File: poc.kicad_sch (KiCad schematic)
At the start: 1 part, among them U1 ESP32-S3-WROOM-1

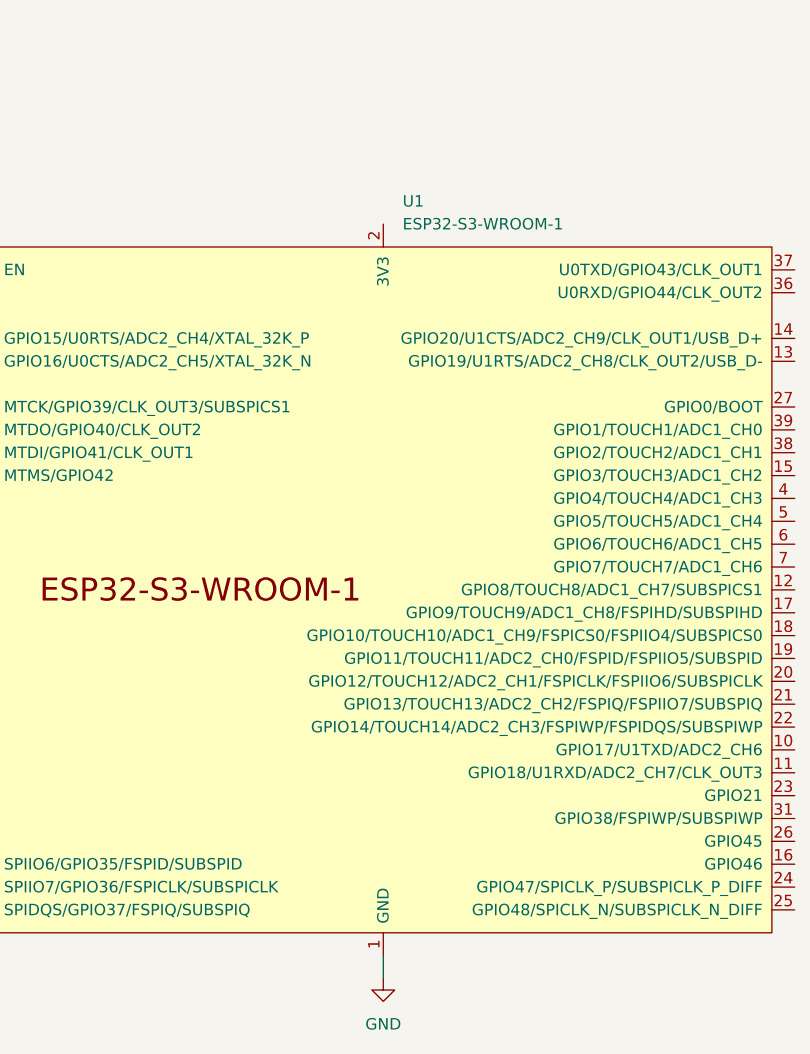
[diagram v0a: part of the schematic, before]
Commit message: POC(schem): add ESP32-S3 power
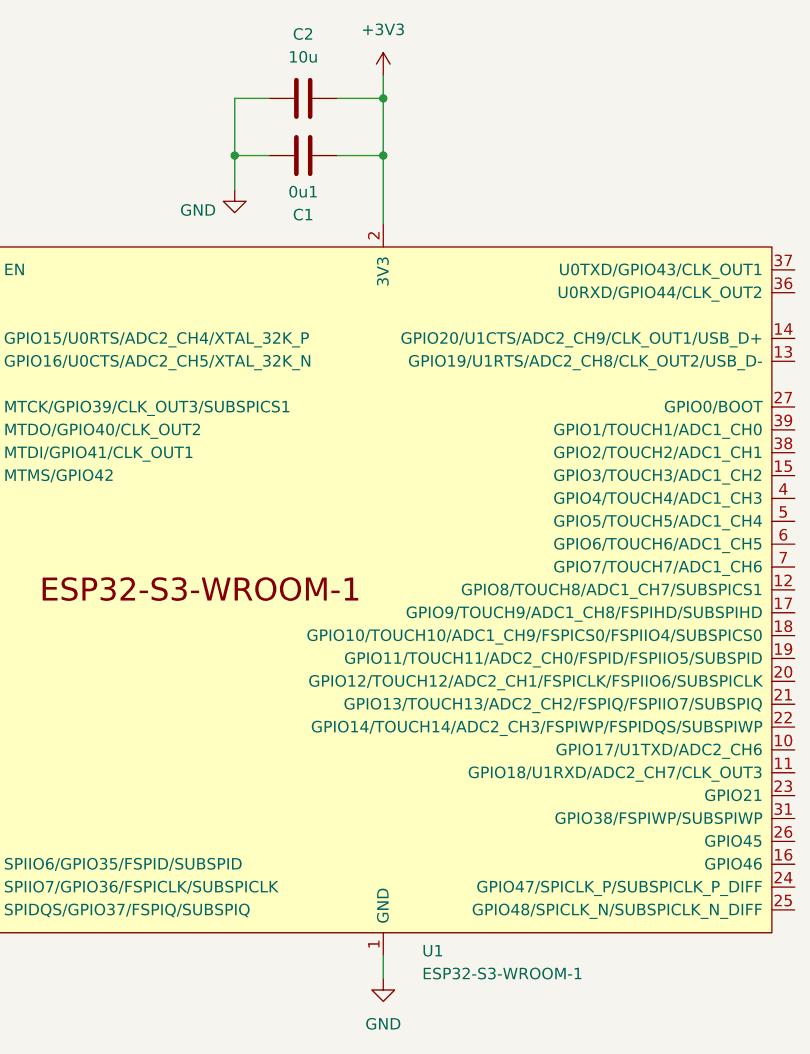
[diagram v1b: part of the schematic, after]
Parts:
- added C1: 0u1, symbol Device:C
- added C2: 10u, symbol Device:C
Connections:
- net GND: now also C1.1, C2.1
- net +3V3: now reaches U1.2 (3V3)
- net +3V3: now also C1.2, C2.2

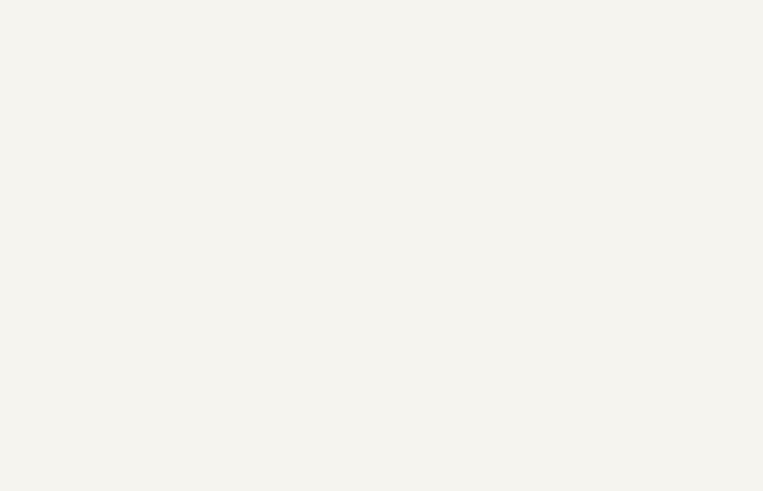
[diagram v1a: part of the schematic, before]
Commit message: POC(schem): add AP7361C 3V3 ldo
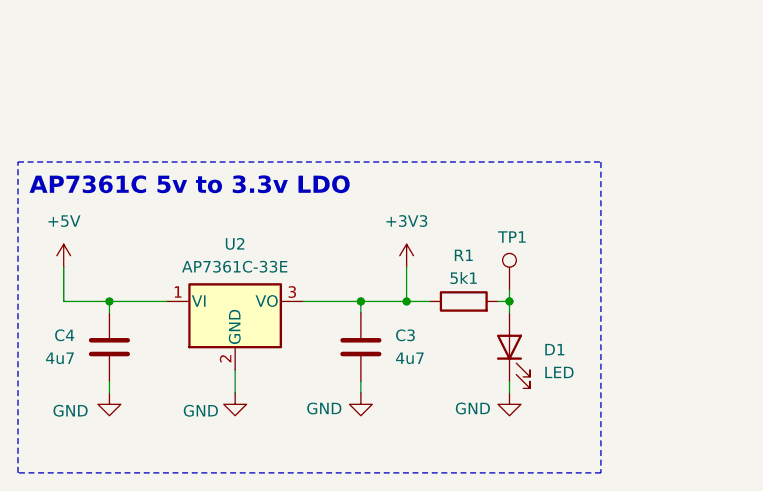
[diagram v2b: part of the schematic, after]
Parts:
- added C3, C4: 4u7, symbol Device:C
- added D1: LED, symbol Device:LED
- added R1: 5k1, symbol Device:R
- added TP1: TestPoint, symbol Connector:TestPoint
- added U2: AP7361C-33E, Package_TO_SOT_SMD:SOT-223-3_TabPin2, symbol Regulator_Linear:AP7361C-33E
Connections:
- net +3V3: now also C3.1, R1.1, U2.3 (VO)
- net GND: now also C3.2, C4.2, D1.1 (K), U2.2 (GND)
- new net: D1.2 (A), R1.2, TP1.1
- new net +5V: C4.1, U2.1 (VI)
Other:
- note added: "AP7361C 5v to 3.3v LDO"

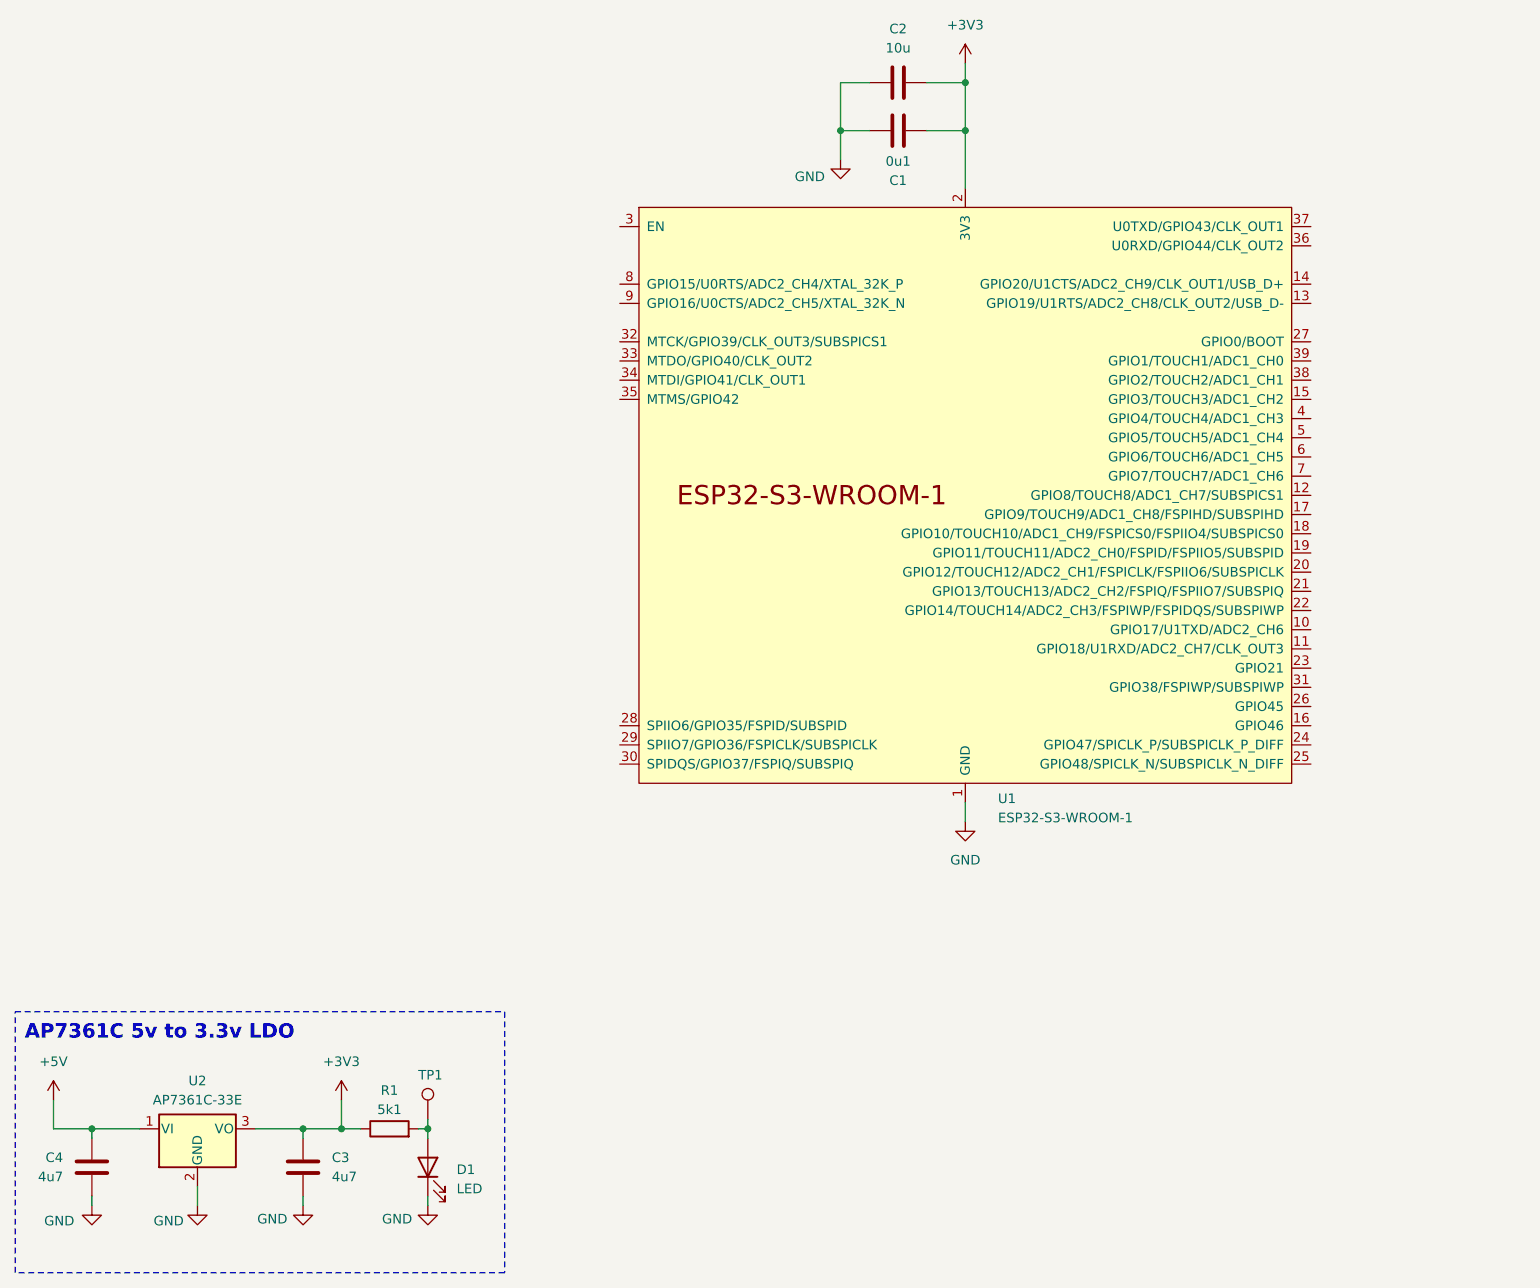
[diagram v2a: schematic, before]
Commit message: POC(schem): add USBC receptacle
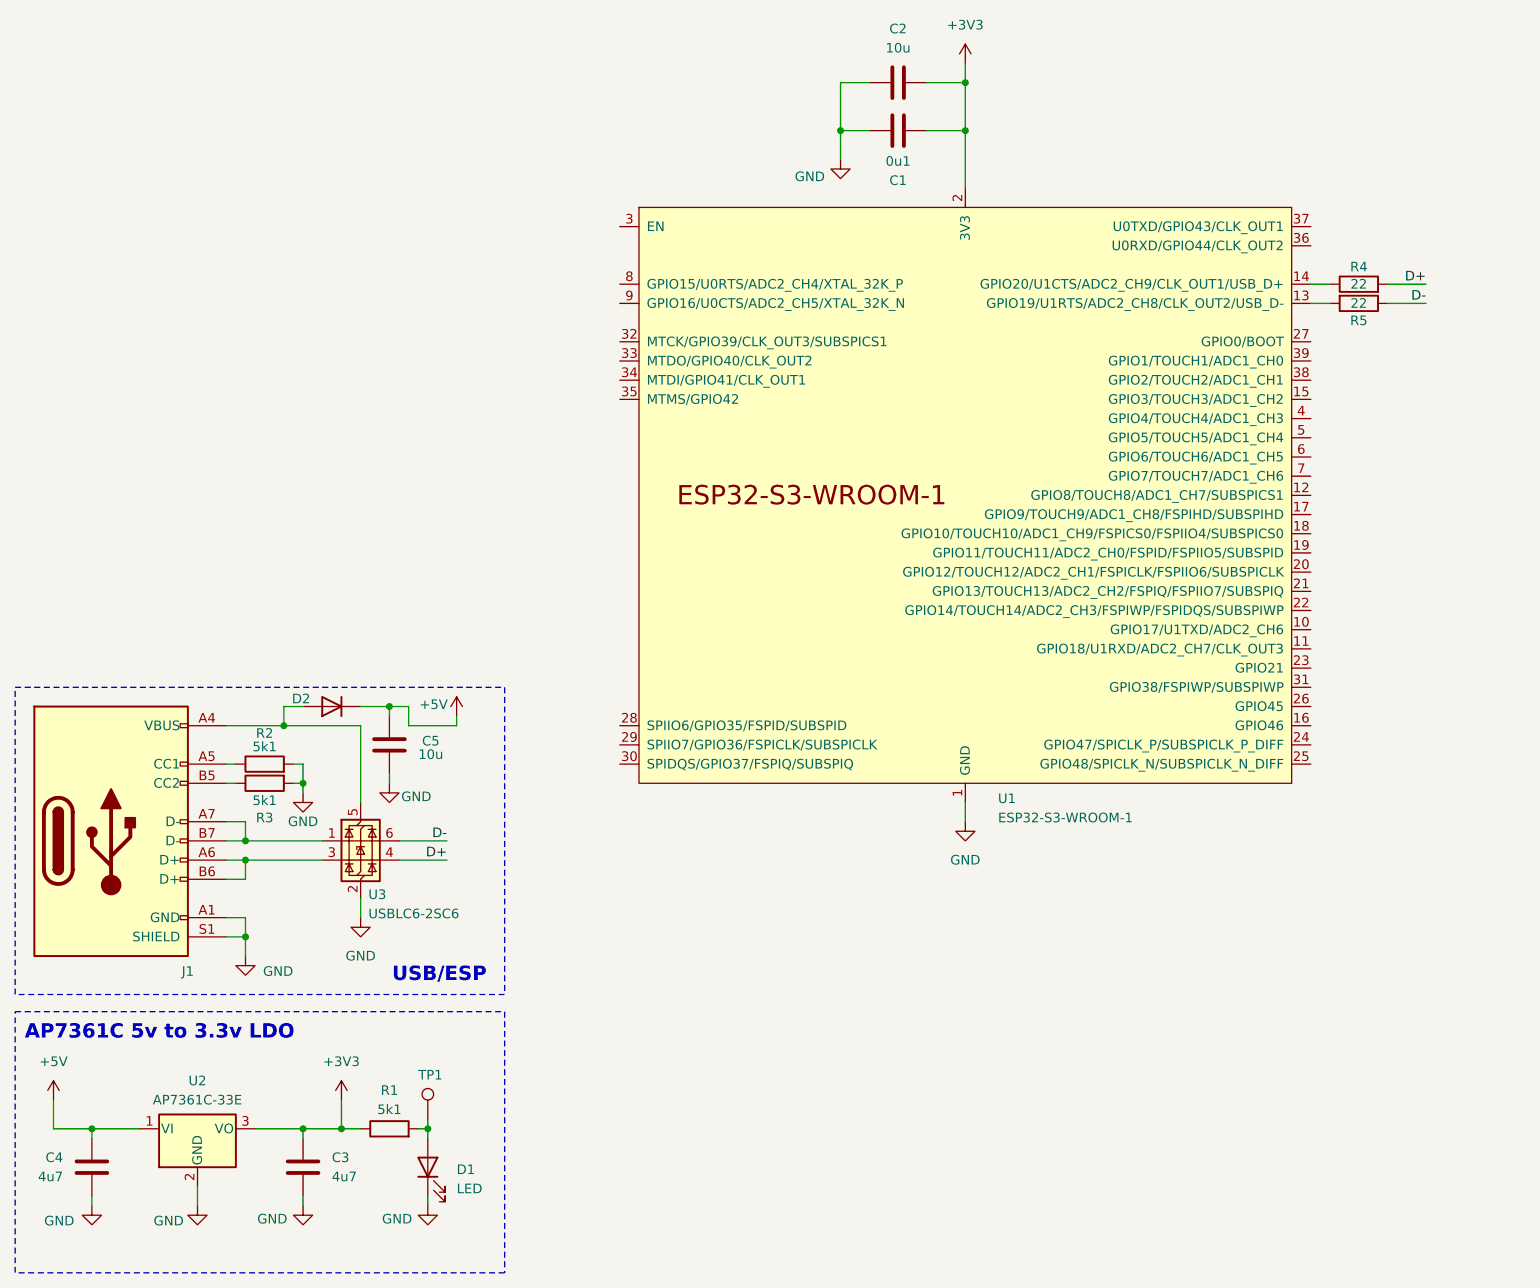
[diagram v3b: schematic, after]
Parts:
- added C5: 10u, symbol Device:C
- added D2: D, symbol Device:D
- added J1: USB_C_Receptacle_USB2.0_14P, symbol Connector:USB_C_Receptacle_USB2.0_14P
- added R2, R3: 5k1, symbol Device:R
- added R4, R5: 22, symbol Device:R
- added U3: USBLC6-2SC6, Package_TO_SOT_SMD:SOT-23-6, symbol Power_Protection:USBLC6-2SC6
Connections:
- net +5V: now also C5.1, D2.1 (K)
- net GND: now also C5.2, J1.A1 (GND), J1.A12 (GND), J1.B1 (GND), J1.B12 (GND), J1.S1 (SHIELD), R2.2, R3.2, U3.2 (GND)
- net at U1.13 (GPIO19/U1RTS/ADC2_CH8/CLK_OUT2/USB_D-): now also R5.2
- net at U1.14 (GPIO20/U1CTS/ADC2_CH9/CLK_OUT1/USB_D+): now also R4.1
- new net: D2.2 (A), J1.A4 (VBUS), J1.A9 (VBUS), J1.B4 (VBUS), J1.B9 (VBUS), U3.5 (VBUS)
- new net: J1.A5 (CC1), R2.1
- new net: J1.A6 (D+), J1.B6 (D+), U3.3 (I/O2)
- new net: J1.A7 (D-), J1.B7 (D-), U3.1 (I/O1)
- new net: J1.B5 (CC2), R3.1
- new net D+: R4.2, U3.4 (I/O2)
- new net D-: R5.1, U3.6 (I/O1)
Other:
- note added: "USB/ESP"

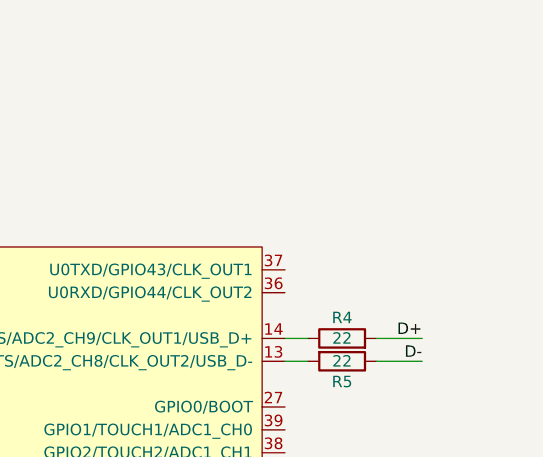
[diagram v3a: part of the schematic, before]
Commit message: POC(schem): add UART connector
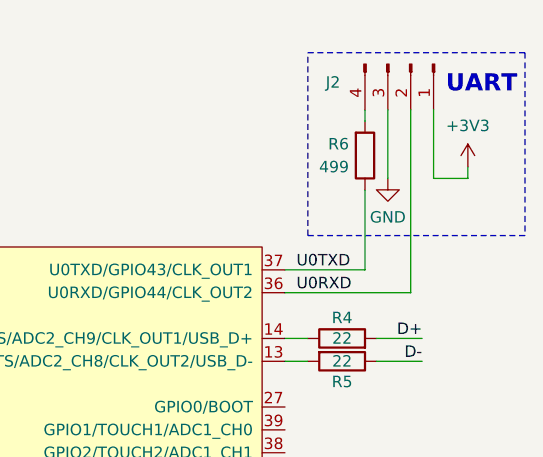
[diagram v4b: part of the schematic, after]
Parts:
- added J2: Conn_01x04_Pin, symbol Connector:Conn_01x04_Pin
- added R6: 499, symbol Device:R
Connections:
- net +3V3: now also J2.1 (Pin_1)
- net GND: now also J2.3 (Pin_3)
- net U0RXD: now reaches U1.36 (U0RXD/GPIO44/CLK_OUT2)
- net U0RXD: now also J2.2 (Pin_2)
- net U0TXD: now reaches U1.37 (U0TXD/GPIO43/CLK_OUT1)
- net U0TXD: now also R6.1
- new net: J2.4 (Pin_4), R6.2
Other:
- note added: "UART"

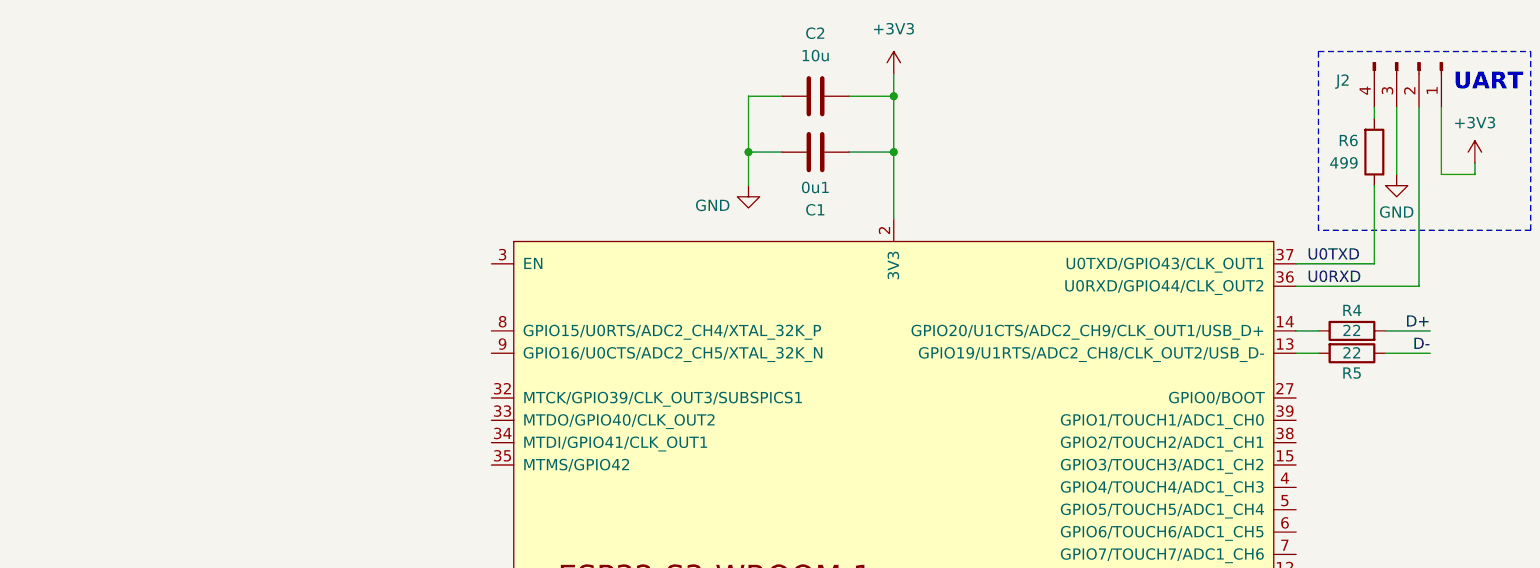
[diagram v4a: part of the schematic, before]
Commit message: POC(schem): fix en delay pin
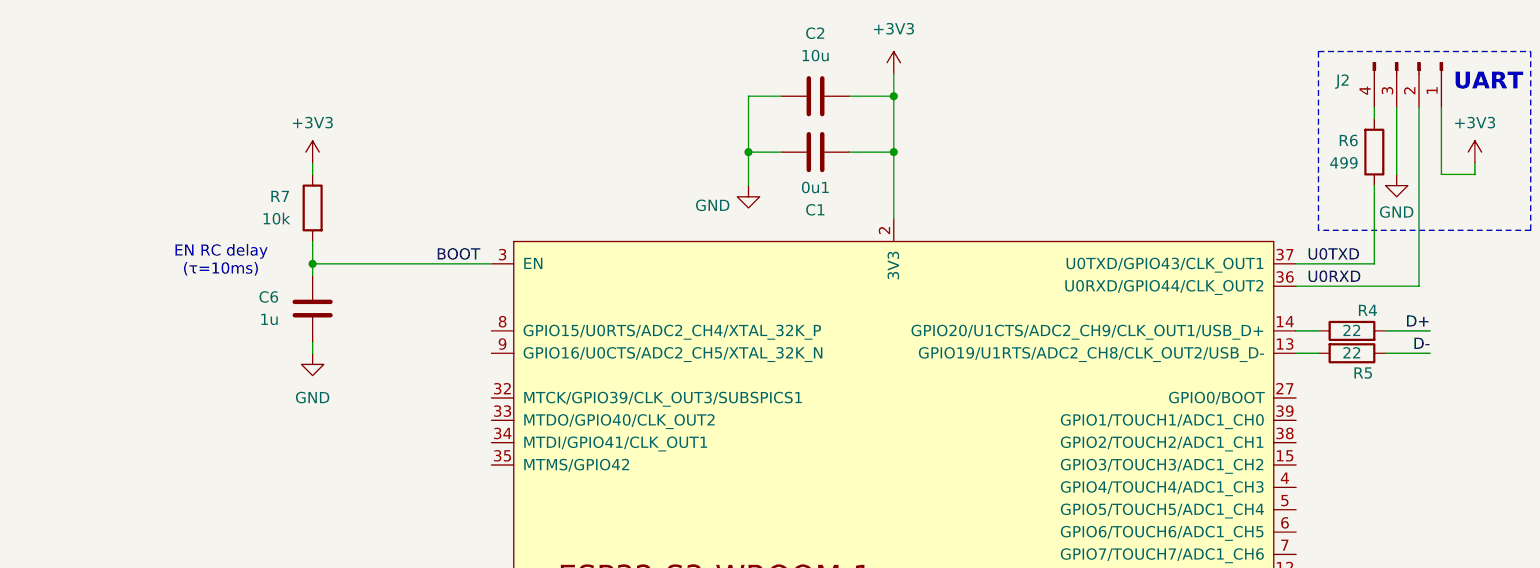
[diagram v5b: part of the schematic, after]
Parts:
- added C6: 1u, symbol Device:C
- added R7: 10k, symbol Device:R
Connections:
- net +3V3: now also R7.1
- net GND: now also C6.2
- net BOOT: now reaches U1.3 (EN)
- net BOOT: now also C6.1, R7.2
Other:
- note added: "EN RC delay (τ=10ms)"

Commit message: POC(schem): add boot and rst btns
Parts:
- added R8: 10k, symbol Device:R
- added SW1, SW2: SW_Push, symbol Switch:SW_Push
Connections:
- net +3V3: now also R8.1
- net BOOT: now also U1.27 (GPIO0/BOOT), R8.2, SW1.2; no longer C6.1, R7.2, U1.3 (EN)
- net GND: now also SW1.1, SW2.1
- new net EN: C6.1, R7.2, SW2.2, U1.3 (EN)
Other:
- note added: "Buttons"
